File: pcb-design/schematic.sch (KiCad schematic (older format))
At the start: 24 parts, among them J1 TempGauge, J2 FuelGauge, J3 SpeedInput_C2_P10-13, J4 Screw_Terminal_01x02, J5 SpeedInput_C2_P10-13, J6 SpeedInput_C2_P10-13, Q1 2N2222, Q2 2N2222, Q3 2N2222, Q6 2N2222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

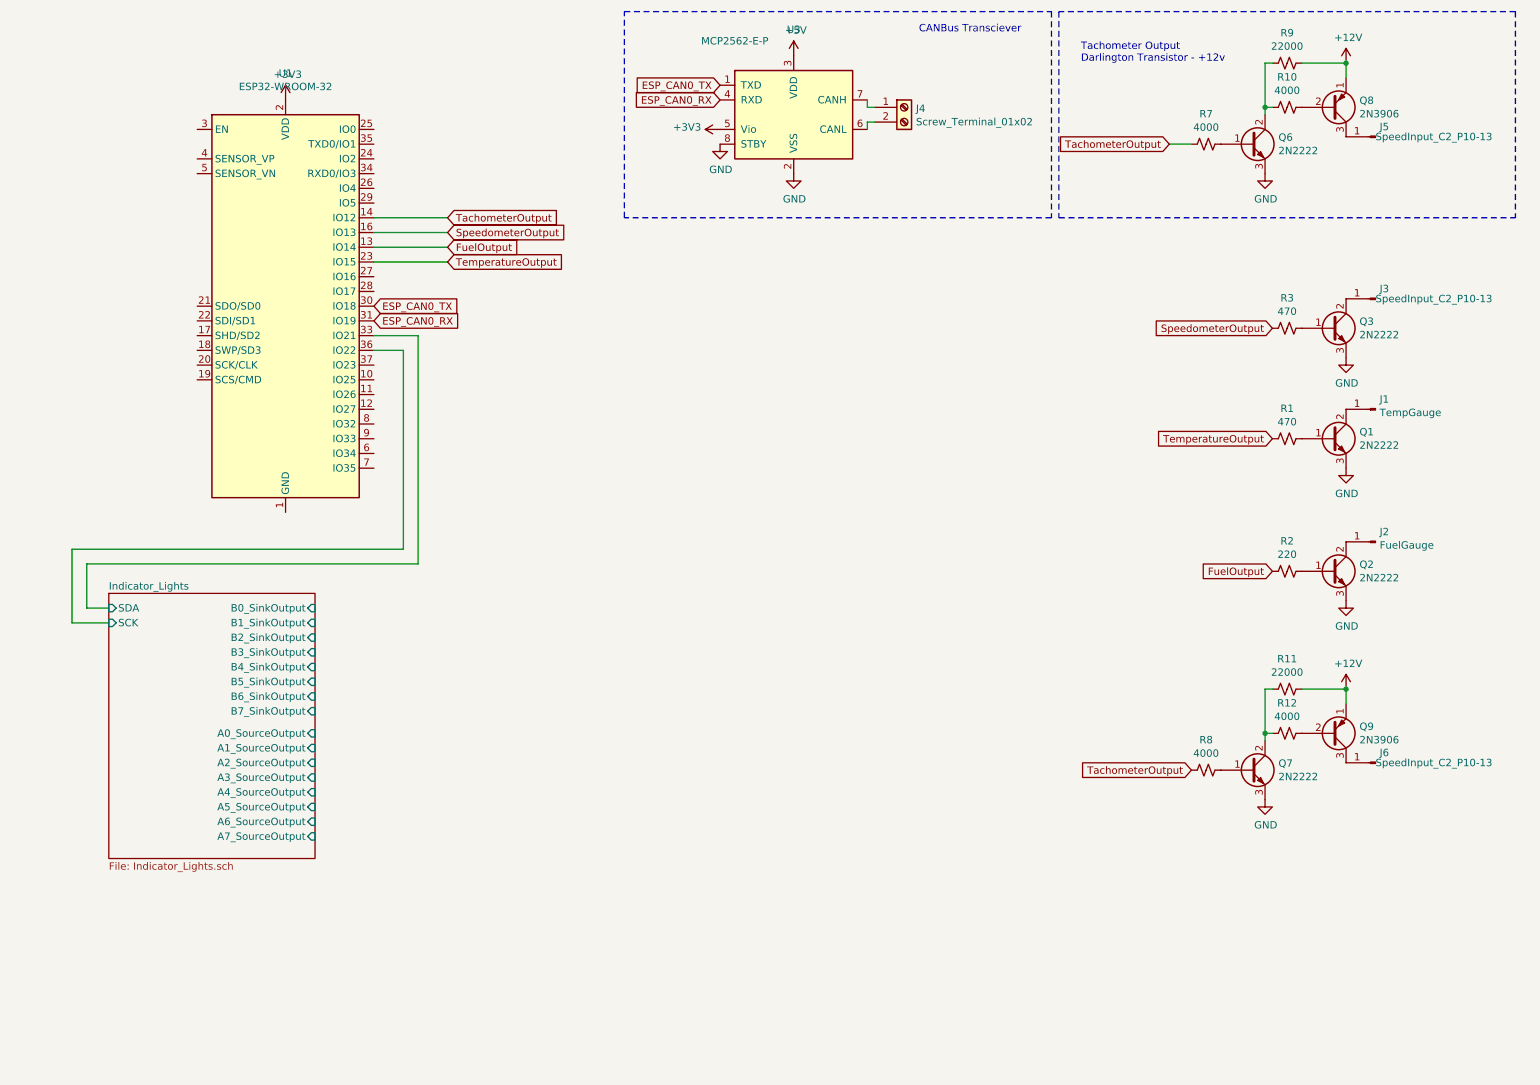
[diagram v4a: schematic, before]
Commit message: Moved some files around
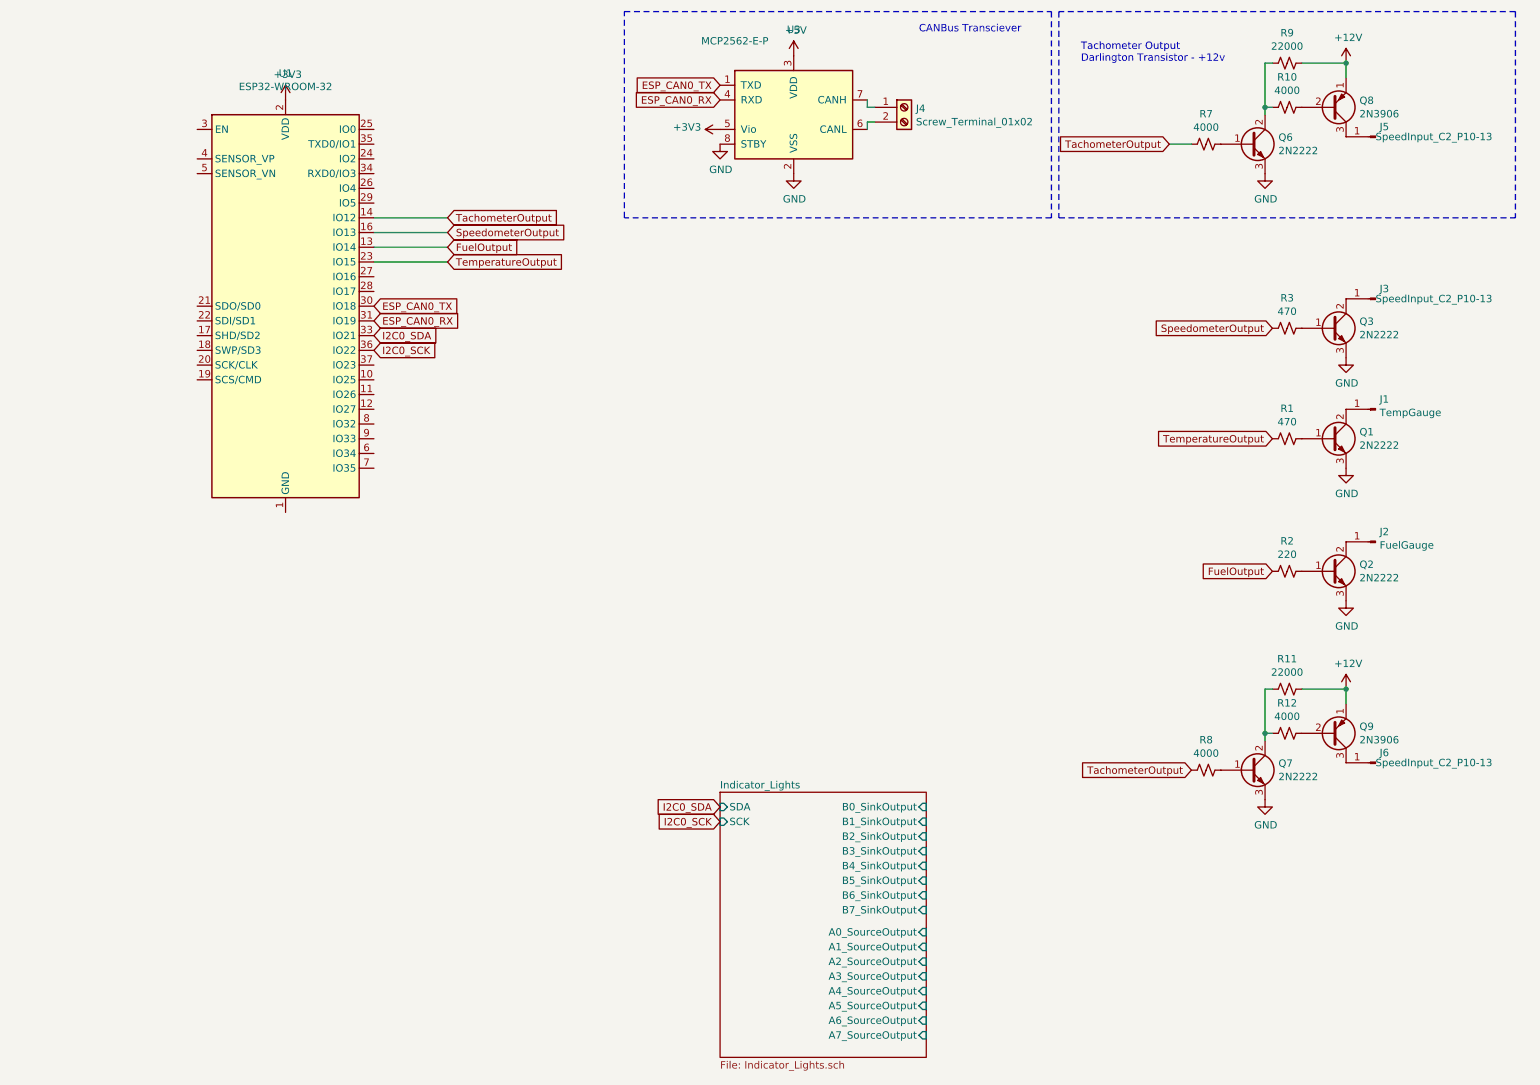
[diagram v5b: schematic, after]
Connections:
- net Indicator_Lights/SCK renamed I2C0_SCK
- net Indicator_Lights/SDA renamed I2C0_SDA
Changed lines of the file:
@@
 	8500 1450 8650 1450
 $Sheet
-S 1300 4500 1400 1800
+S 5450 5850 1400 1800
 U 5E6C532A
 F0 "Indicator_Lights" 50
 F1 "Indicator_Lights.sch" 50
-F2 "SDA" I L 1300 4600 50
-F3 "SCK" I L 1300 4700 50
-F4 "B4_SinkOutput" I R 2700 5000 50
-F5 "B0_SinkOutput" I R 2700 4600 50
-F6 "B1_SinkOutput" I R 2700 4700 50
-F7 "B2_SinkOutput" I R 2700 4800 50
-F8 "B3_SinkOutput" I R 2700 4900 50
-F9 "B5_SinkOutput" I R 2700 5100 50
-F10 "B6_SinkOutput" I R 2700 5200 50
-F11 "B7_SinkOutput" I R 2700 5300 50
-F12 "A0_SourceOutput" I R 2700 5450 50
-F13 "A1_SourceOutput" I R 2700 5550 50
-F14 "A2_SourceOutput" I R 2700 5650 50
-F15 "A3_SourceOutput" I R 2700 5750 50
-F16 "A4_SourceOutput" I R 2700 5850 50
-F17 "A5_SourceOutput" I R 2700 5950 50
-F18 "A6_SourceOutput" I R 2700 6050 50
-F19 "A7_SourceOutput" I R 2700 6150 50
+F2 "SDA" I L 5450 5950 50
+F3 "SCK" I L 5450 6050 50
+F4 "B4_SinkOutput" I R 6850 6350 50
+F5 "B0_SinkOutput" I R 6850 5950 50
+F6 "B1_SinkOutput" I R 6850 6050 50
+F7 "B2_SinkOutput" I R 6850 6150 50
+F8 "B3_SinkOutput" I R 6850 6250 50
+F9 "B5_SinkOutput" I R 6850 6450 50
+F10 "B6_SinkOutput" I R 6850 6550 50
+F11 "B7_SinkOutput" I R 6850 6650 50
+F12 "A0_SourceOutput" I R 6850 6800 50
+F13 "A1_SourceOutput" I R 6850 6900 50
+F14 "A2_SourceOutput" I R 6850 7000 50
+F15 "A3_SourceOutput" I R 6850 7100 50
+F16 "A4_SourceOutput" I R 6850 7200 50
+F17 "A5_SourceOutput" I R 6850 7300 50
+F18 "A6_SourceOutput" I R 6850 7400 50
+F19 "A7_SourceOutput" I R 6850 7500 50
 $EndSheet
-Wire Wire Line
-	1300 4600 1150 4600
-Wire Wire Line
-	1150 4600 1150 4300
-Wire Wire Line
-	1150 4300 3400 4300
-Wire Wire Line
-	3400 4300 3400 2750
-Wire Wire Line
-	3400 2750 3100 2750
-Wire Wire Line
-	3100 2850 3300 2850
-Wire Wire Line
-	3300 2850 3300 4200
-Wire Wire Line
-	3300 4200 1050 4200
-Wire Wire Line
-	1050 4200 1050 4700
-Wire Wire Line
-	1050 4700 1300 4700
 Wire Wire Line
 	3100 1950 3600 1950
@@
 Wire Notes Line
 	7750 550  7750 1950
+Text GLabel 3100 2750 2    50   Input ~ 0
+I2C0_SDA
+Text GLabel 3100 2850 2    50   Input ~ 0
+I2C0_SCK
+Text GLabel 5450 5950 0    50   Input ~ 0
+I2C0_SDA
+Text GLabel 5450 6050 0    50   Input ~ 0
+I2C0_SCK
 $EndSCHEMATC

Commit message: Swapped the esp32 symbol and footprint to be one for the dev modules so I can just populate the boards with standoffs.
Wired up some more nets and made the layout a little prettier.
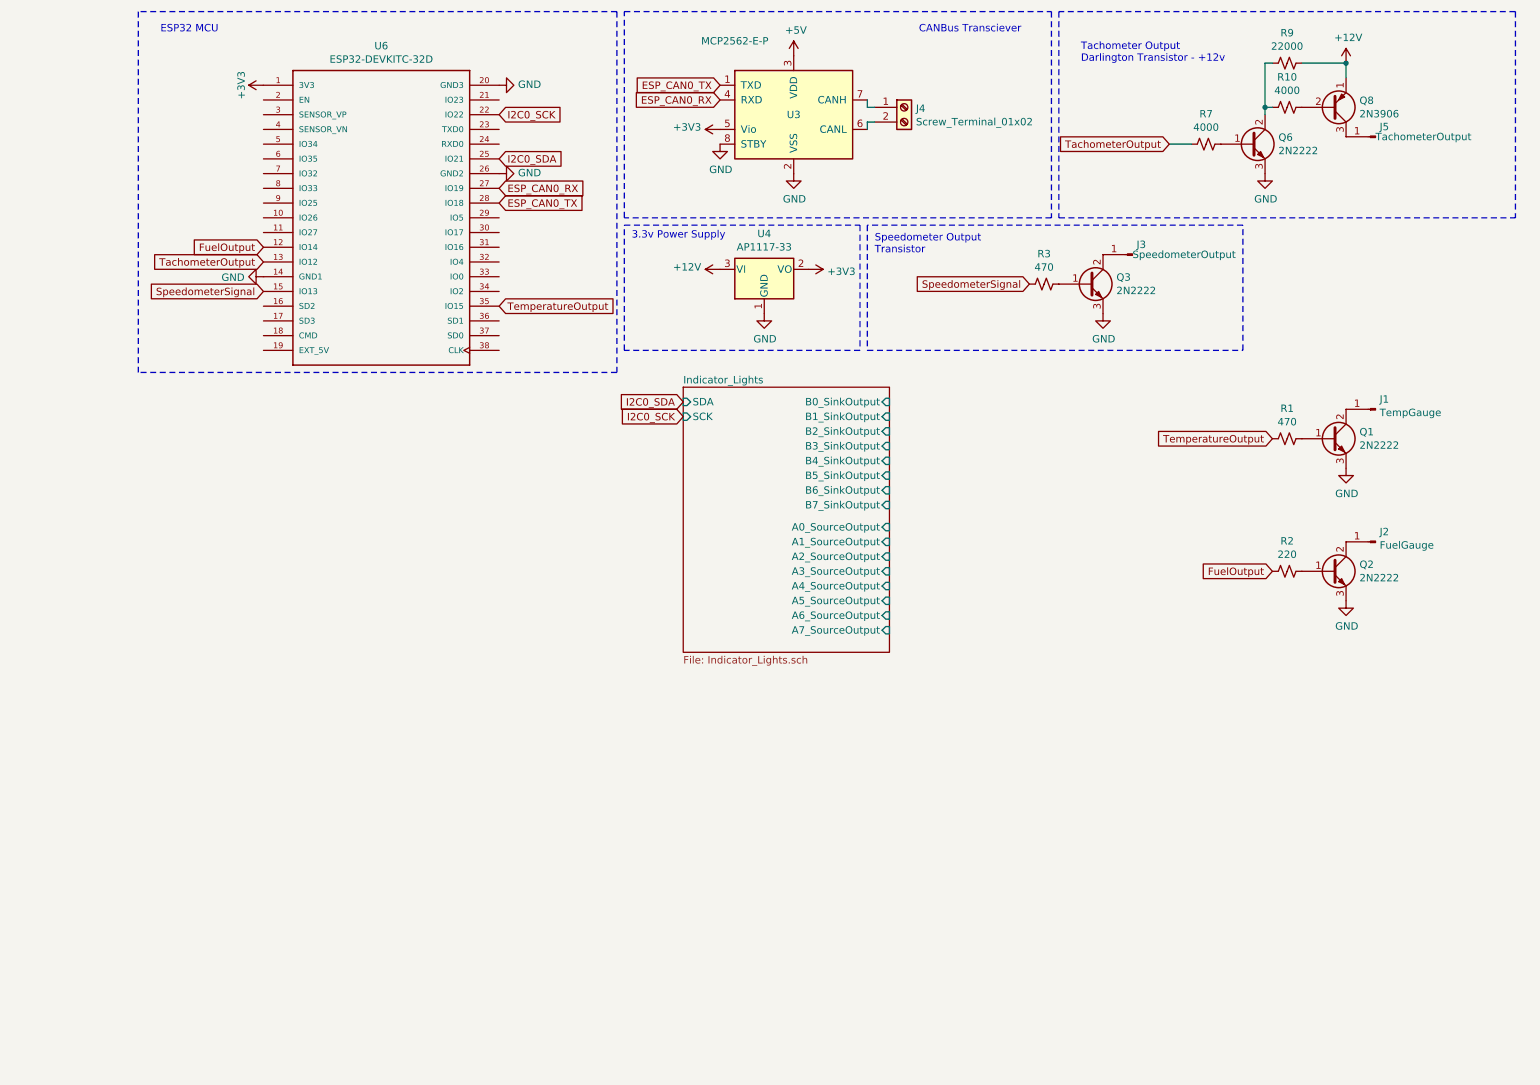
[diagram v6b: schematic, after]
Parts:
- removed J6: SpeedInput_C2_P10-13, TestPoint:TestPoint_Pad_D2.5mm, symbol Connector:Conn_01x01_Male
- removed Q7: 2N2222, Package_TO_SOT_THT:TO-92_HandSolder, symbol Device:Q_NPN_BCE
- removed Q9: 2N3906, Package_TO_SOT_THT:TO-92_Inline, symbol Transistor_BJT:2N3906
- removed R11: 22000, Resistor_SMD:R_1206_3216Metric_Pad1.42x1.75mm_HandSolder, symbol Device:R_Small_US
- removed R12, R8: 4000, Resistor_SMD:R_1206_3216Metric_Pad1.42x1.75mm_HandSolder, symbol Device:R_Small_US
- removed U1: ESP32-WROOM-32, RF_Module:ESP32-WROOM-32, symbol schematic-rescue:ESP32-WROOM-32-RF_Module
- added U4: AP1117-33, Package_TO_SOT_SMD:SOT-223-3_TabPin2, symbol Regulator_Linear:AP1117-33
- added U6: ESP32-DEVKITC-32D, MODULE_ESP32-DEVKITC-32D, symbol ESP32-DEVKITC-32D:ESP32-DEVKITC-32D
- J3: value SpeedInput_C2_P10-13 -> SpeedometerOutput
- J4: footprint (none) -> TerminalBlock_TE-Connectivity:TerminalBlock_TE_282834-2_1x02_P2.54mm_Horizontal
- J5: value SpeedInput_C2_P10-13 -> TachometerOutput
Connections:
- net +12V: now also U4.3 (VI)
- net +3V3: now also U4.2 (VO), U6.1 (3V3)
- net ESP_CAN0_RX: now also U6.27 (IO19)
- net ESP_CAN0_TX: now also U6.28 (IO18)
- net FuelOutput: now also U6.12 (IO14)
- net GND: now also U4.1 (GND), U6.14 (GND1), U6.20 (GND3), U6.26 (GND2)
- net I2C0_SCK: now also U6.22 (IO22)
- net I2C0_SDA: now also U6.25 (IO21)
- net TachometerOutput: now also U6.13 (IO12)
- net TemperatureOutput: now also U6.35 (IO15)
- net SpeedometerOutput renamed SpeedometerSignal
- net SpeedometerSignal: now also U6.15 (IO13)
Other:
- note added: "3.3v Power Supply\n"
- note added: "ESP32 MCU"
- note added: "Speedometer Output\nTransistor"
- moved on the sheet: J3, Q3, R3

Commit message: Added TE 827881-1 connector and footprint re-arranged schematic
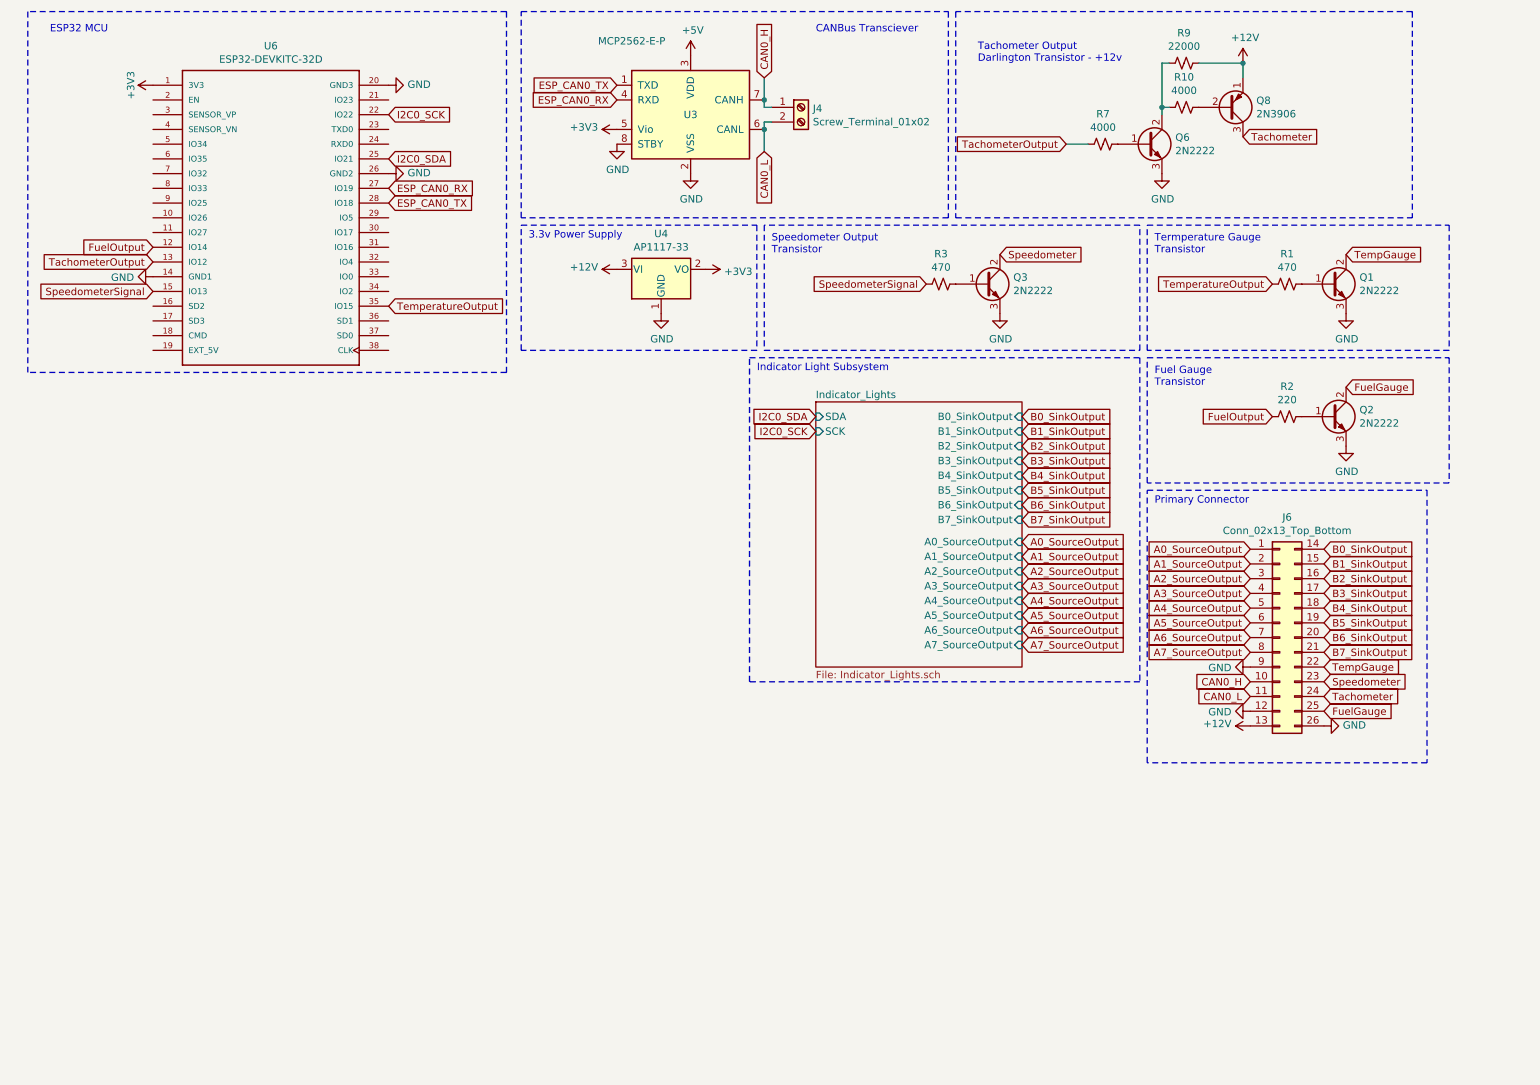
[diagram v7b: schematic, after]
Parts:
- removed J1: TempGauge, TestPoint:TestPoint_Pad_D2.5mm, symbol Connector:Conn_01x01_Male
- removed J2: FuelGauge, TestPoint:TestPoint_Pad_D2.5mm, symbol Connector:Conn_01x01_Male
- removed J3: SpeedometerOutput, TestPoint:TestPoint_Pad_D2.5mm, symbol Connector:Conn_01x01_Male
- removed J5: TachometerOutput, TestPoint:TestPoint_Pad_D2.5mm, symbol Connector:Conn_01x01_Male
- added J6: Conn_02x13_Top_Bottom, pcb-design:Connector_TE_827881-1, symbol Connector_Generic:Conn_02x13_Top_Bottom
- U6: footprint MODULE_ESP32-DEVKITC-32D -> pcb-design:MODULE_ESP32-DEVKITC-32D
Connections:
- net +12V: now also J6.13 (Pin_13)
- net GND: now also J6.12 (Pin_12), J6.26 (Pin_26), J6.9 (Pin_9)
- net FuelGauge: now reaches Q2.2 (C)
- net FuelGauge: now also J6.25 (Pin_25)
- net TempGauge: now reaches Q1.2 (C)
- net TempGauge: now also J6.22 (Pin_22)
- net Speedometer: now reaches Q3.2 (C)
- net Speedometer: now also J6.23 (Pin_23)
- net Tachometer: now reaches Q8.3 (C)
- net Tachometer: now also J6.24 (Pin_24)
- net CAN0_H: now reaches J4.1 (Pin_1), U3.7 (CANH)
- net CAN0_H: now also J6.10 (Pin_10)
- net CAN0_L: now reaches J4.2 (Pin_2), U3.6 (CANL)
- net CAN0_L: now also J6.11 (Pin_11)
- new net A0_SourceOutput: J6.1 (Pin_1)
- new net A1_SourceOutput: J6.2 (Pin_2)
- new net A2_SourceOutput: J6.3 (Pin_3)
- new net A3_SourceOutput: J6.4 (Pin_4)
- new net A4_SourceOutput: J6.5 (Pin_5)
- new net A5_SourceOutput: J6.6 (Pin_6)
- new net A6_SourceOutput: J6.7 (Pin_7)
- new net A7_SourceOutput: J6.8 (Pin_8)
- new net B0_SinkOutput: J6.14 (Pin_14)
- new net B1_SinkOutput: J6.15 (Pin_15)
- new net B2_SinkOutput: J6.16 (Pin_16)
- new net B3_SinkOutput: J6.17 (Pin_17)
- new net B4_SinkOutput: J6.18 (Pin_18)
- new net B5_SinkOutput: J6.19 (Pin_19)
- new net B6_SinkOutput: J6.20 (Pin_20)
- new net B7_SinkOutput: J6.21 (Pin_21)
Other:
- note added: "Fuel Gauge \nTransistor\n"
- note added: "Indicator Light Subsystem"
- note added: "Primary Connector\n"
- note added: "Termperature Gauge\nTransistor\n"
- moved on the sheet: J4, Q1, Q2, Q3, Q6, Q8, R1, R10, R2, R3, R7, R9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
